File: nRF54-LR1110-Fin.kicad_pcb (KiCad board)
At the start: 2 copper layers, 8 parts, among them U1 LR1110IMLTRT, U2 SKY13380-350LF, Y1 TG2520SMN 32.0000M-MCGNNM3

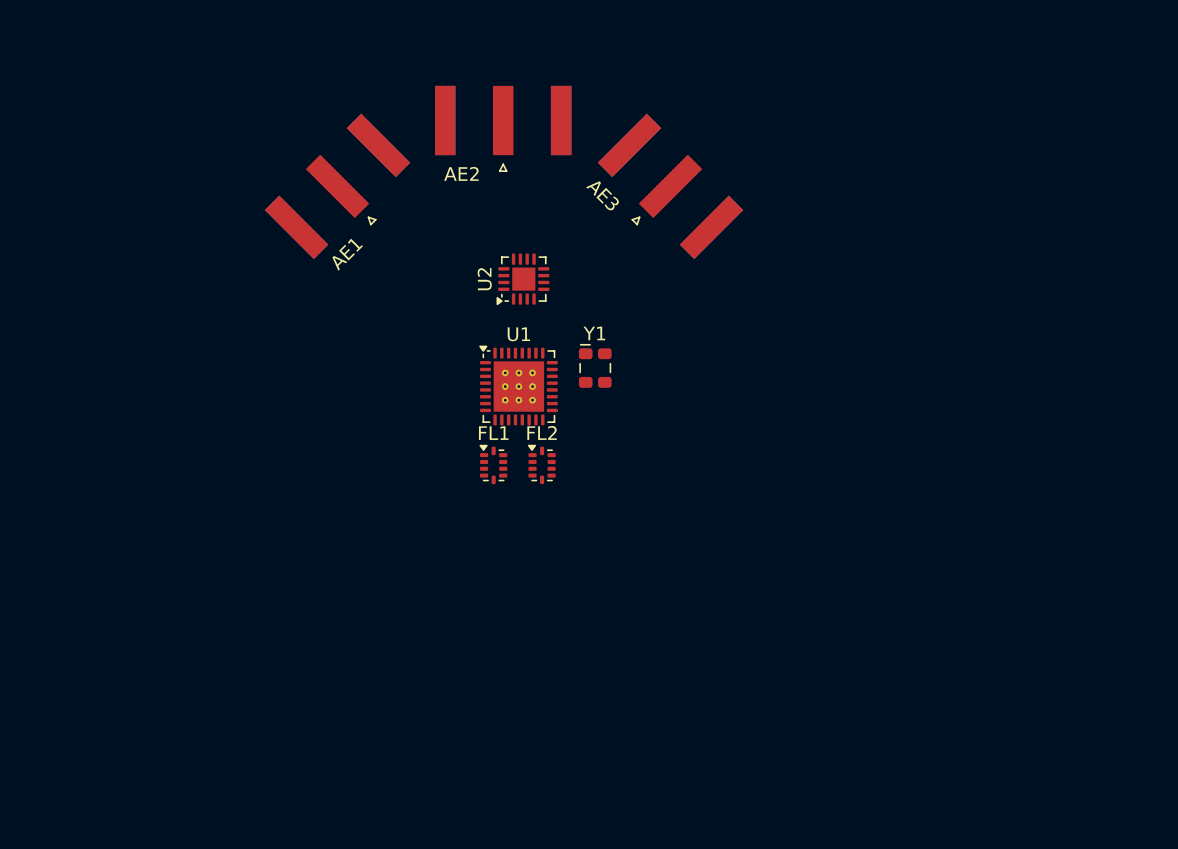
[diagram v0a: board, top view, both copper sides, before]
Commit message: schematic: add level shifter, gnss amp
Adds level shifter to L15-DK, GNSS amplifier, proper handling of RF
components for LoRA radio, initial board outline.

Signed-off-by: Helmut Lord <kellyhlord@gmail.com>
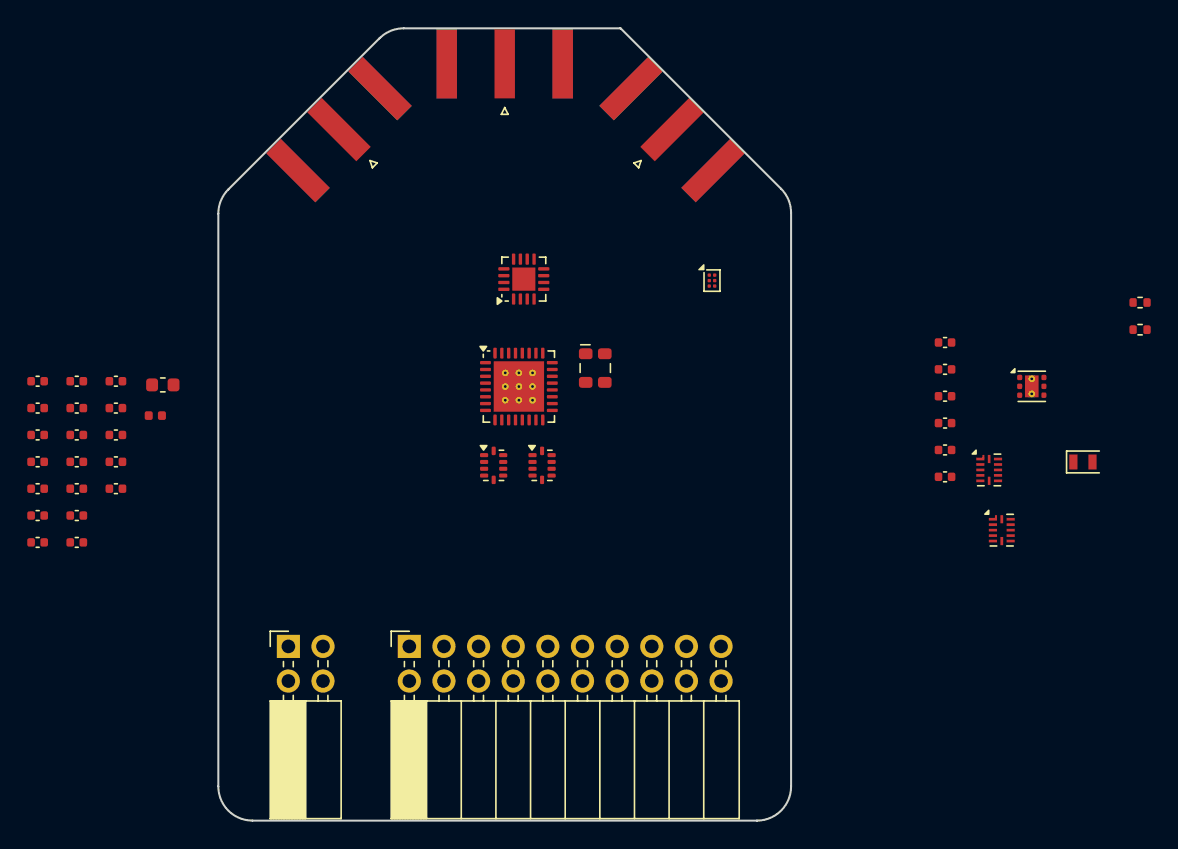
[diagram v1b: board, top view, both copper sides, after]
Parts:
- added C1: 470nF, Capacitor_SMD:C_0402_1005Metric, F.Cu at (106.2, 108.3)
- added C10: 100nF, Capacitor_SMD:C_0402_1005Metric, F.Cu at (109.1, 112.2)
- added C11: 100nF, Capacitor_SMD:C_0402_1005Metric, F.Cu at (172.8, 105.4)
- added C12: 100nF, Capacitor_SMD:C_0402_1005Metric, F.Cu at (172.8, 107.4)
- added C13: 1uF, Capacitor_SMD:C_0402_1005Metric, F.Cu at (172.8, 109.4)
- added C14: 1uF, Capacitor_SMD:C_0402_1005Metric, F.Cu at (172.8, 111.3)
- added C15: 100nF, Capacitor_SMD:C_0402_1005Metric, F.Cu at (172.8, 113.3)
- added C16: 100nF, Capacitor_SMD:C_0402_1005Metric, F.Cu at (172.8, 115.3)
- added C2: 100nF, Capacitor_SMD:C_0402_1005Metric, F.Cu at (106.2, 110.2)
- added C3: 100nF, Capacitor_SMD:C_0402_1005Metric, F.Cu at (106.2, 112.2)
- added C4: 47pF, Capacitor_SMD:C_0402_1005Metric, F.Cu at (106.2, 114.2)
- added C5: 100nF, Capacitor_SMD:C_0402_1005Metric, F.Cu at (106.2, 116.2)
- added C6: 12pF, Capacitor_SMD:C_0402_1005Metric, F.Cu at (106.2, 118.1)
- added C7: 12pF, Capacitor_SMD:C_0402_1005Metric, F.Cu at (106.2, 120.1)
- added C8: 100nF, Capacitor_SMD:C_0402_1005Metric, F.Cu at (109.1, 108.3)
- added C9: 1nF, Capacitor_SMD:C_0402_1005Metric, F.Cu at (109.1, 110.2)
- added GPIO1: Conn_02x10_Odd_Even, Connector_PinSocket_2.54mm:PinSocket_2x10_P2.54mm_Horizontal, F.Cu at (133.5, 127.7)
- added L1: 15uH, Inductor_SMD:L_0603_1608Metric, F.Cu at (115.4, 108.5)
- added L2: 12nH, Inductor_SMD:L_0402_1005Metric, F.Cu at (114.9, 110.8)
- added R1: 100kR, Resistor_SMD:R_0402_1005Metric, F.Cu at (187.1, 102.5)
- added R2: 100kR, Resistor_SMD:R_0402_1005Metric, F.Cu at (187.1, 104.5)
- added U3: BGA535N6, Package_LGA:Infineon_PG-TSNP-6-10_0.7x1.1mm_0.7x1.1mm_P0.4mm, F.Cu at (155.7, 100.9)
- added U4: TXB0104RUT, Package_DFN_QFN:Texas_R-PUQFN-N12, F.Cu at (176.0, 114.8)
- added U5: TLV75533PDRV, Package_SON:WSON-6-1EP_2x2mm_P0.65mm_EP1x1.6mm_ThermalVias, F.Cu at (179.2, 108.7)
- added U6: TXB0104RUT, Package_DFN_QFN:Texas_R-PUQFN-N12, F.Cu at (176.9, 119.2)
- added VSUP1: Conn_02x02_Odd_Even, Connector_PinSocket_2.54mm:PinSocket_2x02_P2.54mm_Horizontal, F.Cu at (124.6, 127.7)
- added Y2: 32.768KHz, Crystal:Crystal_SMD_2012-2Pin_2.0x1.2mm, F.Cu at (182.9, 114.2)
- added Z1: R_Small, Capacitor_SMD:C_0402_1005Metric, F.Cu at (109.1, 114.2)
- added Z2: R_Small, Capacitor_SMD:C_0402_1005Metric, F.Cu at (109.1, 116.2)
- added Z3: R_Small, Capacitor_SMD:C_0402_1005Metric, F.Cu at (109.1, 118.1)
- added Z4: R_Small, Capacitor_SMD:C_0402_1005Metric, F.Cu at (109.1, 120.1)
- added Z5: R_Small, Capacitor_SMD:C_0402_1005Metric, F.Cu at (112.0, 108.3)
- added Z6: R_Small, Capacitor_SMD:C_0402_1005Metric, F.Cu at (112.0, 110.2)
- added Z7: R_Small, Capacitor_SMD:C_0402_1005Metric, F.Cu at (112.0, 112.2)
- added Z8: R_Small, Capacitor_SMD:C_0402_1005Metric, F.Cu at (112.0, 114.2)
- added Z9: R_Small, Capacitor_SMD:C_0402_1005Metric, F.Cu at (112.0, 116.2)
- moved AE2 4.16 mm to (140.5, 85.0)
- moved AE3 4.16 mm to (152.8, 89.8)
- moved AE1 4.16 mm to (128.4, 89.8)
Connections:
- AE1 pad 1: unconnected-(AE1-A-Pad1) -> Net-(AE1-A)
- AE1 pad 2: unconnected-(AE1-Shield-Pad2) -> GND
- AE2 pad 1: unconnected-(AE2-A-Pad1) -> Net-(AE2-A)
- AE2 pad 2: unconnected-(AE2-Shield-Pad2) -> GND
- AE3 pad 1: unconnected-(AE3-A-Pad1) -> Net-(AE3-A)
- AE3 pad 2: unconnected-(AE3-Shield-Pad2) -> GND
- FL2 pad 7: unconnected-(FL2-WIFI-Pad7) -> Net-(FL2-WIFI)
- FL2 pad 8: unconnected-(FL2-GNSS-Pad8) -> Net-(FL2-GNSS)
- U1 pad 10: unconnected-(U1-DIO8-Pad10) -> /GNSSLP2
- U1 pad 11: unconnected-(U1-DIO7-Pad11) -> /GNSSLP1
- U1 pad 15: Net-(U1-VBAT) -> VDD
- U1 pad 19: unconnected-(U1-DIO6-Pad19) -> /RFSW2
- U1 pad 2: Net-(U1-VBAT) -> VDD
- U1 pad 20: unconnected-(U1-DIO5-Pad20) -> /RFSW1
- U1 pad 23: /P1.04 -> /PCK
- U1 pad 24: /P1.07 -> /~{CS}
- U1 pad 3: Net-(U1-VTCXO) -> VDD
- U1 pad 6: /P1.10 -> /~{RESET}
- U2 pad 11: unconnected-(U2-ANT-Pad11) -> Net-(U2-ANT)
- U2 pad 2: unconnected-(U2-VDD-Pad2) -> VDD
- U2 pad 3: unconnected-(U2-CTRL2-Pad3) -> /RFSW2
- U2 pad 4: unconnected-(U2-CTRL1-Pad4) -> /RFSW1
- Y1 pad 4: Net-(U1-VTCXO) -> VDD
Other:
- board outline added: 42 x 58.1 mm
